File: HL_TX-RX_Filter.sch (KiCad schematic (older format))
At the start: 209 parts, among them J1 CNR1, J10 To Rx in, J11 CONN_01X03, J12 + - 12v, J2 CNR3, J3 Antenna, J4 CNR2, J5 CNR4, J6 From Tx, J7 ICSP, J8 CONN_01X05, J9 SCL SDA, Q1 2N7002, Q2 2N7002, Q3 2N7002, Q4 2N7002, Q5 2N7002, Q6 2N7002, Q7 2N7002, Q8 2N7002, U1 ATMEGA328-AU, U10 PE4259, U11 PE4259, U12 PE4259, U2 PE4259, U3 PE4259, U4 PE4259, U5 PE4259, U6 PE4259, U7 PE4259, U8 PE4259, U9 PE4259

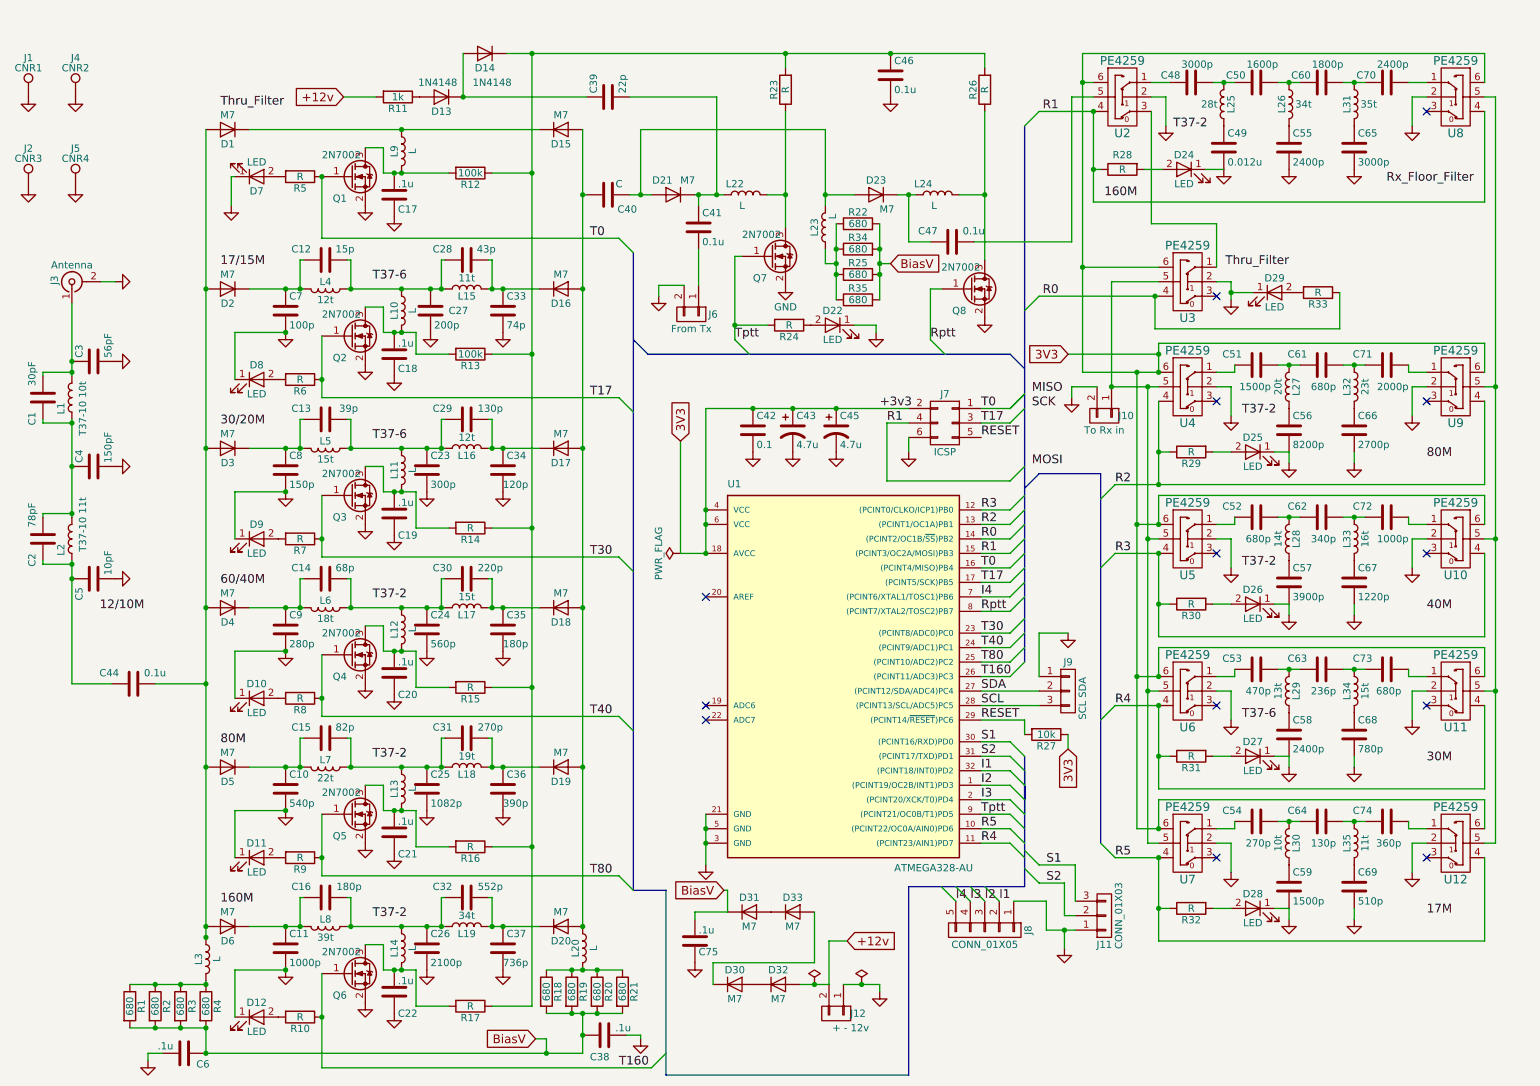
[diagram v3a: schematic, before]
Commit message: Got last of components placed on board
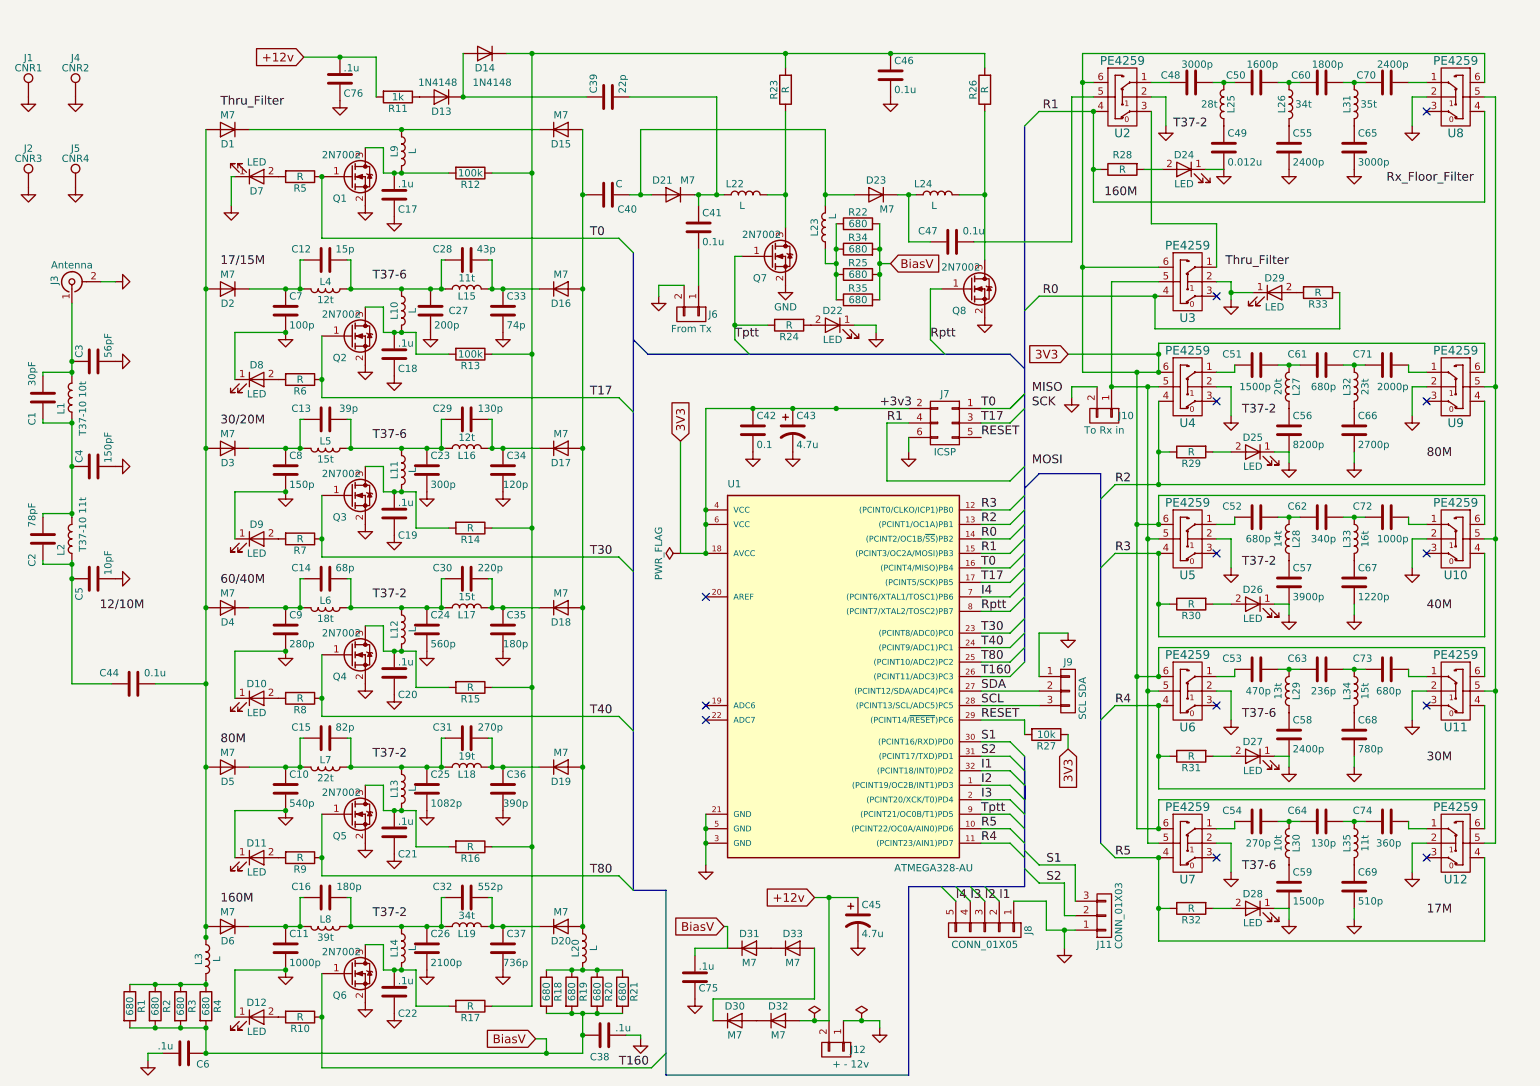
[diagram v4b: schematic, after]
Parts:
- added C76: .1u, Capacitors_SMD:C_1206_HandSoldering, symbol C
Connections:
- net +12v: now also C45.1, C76.1
- net 3V3: no longer C45.1
- net GND: now also C76.2
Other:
- moved on the sheet: C45, C75, D30, D31, D32, D33, J12
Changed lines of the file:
@@
 L PWR_FLAG #FLG050
 U 1 1 59199696
-P 6150 7025
-F 0 "#FLG050" H 6150 7100 50  0001 C CNN
-F 1 "PWR_FLAG" H 6150 7175 50  0001 C CNN
-F 2 "" H 6150 7025 50  0001 C CNN
-F 3 "" H 6150 7025 50  0001 C CNN
-	1    6150 7025
+P 6150 7275
+F 0 "#FLG050" H 6150 7350 50  0001 C CNN
+F 1 "PWR_FLAG" H 6150 7425 50  0001 C CNN
+F 2 "" H 6150 7275 50  0001 C CNN
+F 3 "" H 6150 7275 50  0001 C CNN
+	1    6150 7275
 	1    0    0    -1
 $EndComp
@@
 L CP1 C45
 U 1 1 591F53E3
-P 6300 3200
-F 0 "C45" H 6325 3300 50  0000 L CNN
-F 1 "4.7u" H 6325 3100 50  0000 L CNN
-F 2 "Capacitors_THT:CP_Radial_D5.0mm_P2.00mm" H 6300 3200 50  0001 C CNN
-F 3 "" H 6300 3200 50  0001 C CNN
-	1    6300 3200
+P 6450 6575
+F 0 "C45" H 6475 6675 50  0000 L CNN
+F 1 "4.7u" H 6475 6475 50  0000 L CNN
+F 2 "Capacitors_THT:CP_Radial_D5.0mm_P2.00mm" H 6450 6575 50  0001 C CNN
+F 3 "" H 6450 6575 50  0001 C CNN
+	1    6450 6575
 	1    0    0    -1
 $EndComp
@@
 L GND #PWR055
 U 1 1 591F5DC7
-P 6300 3350
-F 0 "#PWR055" H 6300 3100 50  0001 C CNN
-F 1 "GND" H 6300 3200 50  0001 C CNN
-F 2 "" H 6300 3350 50  0001 C CNN
-F 3 "" H 6300 3350 50  0001 C CNN
-	1    6300 3350
+P 6450 6725
+F 0 "#PWR055" H 6450 6475 50  0001 C CNN
+F 1 "GND" H 6450 6575 50  0001 C CNN
+F 2 "" H 6450 6725 50  0001 C CNN
+F 3 "" H 6450 6725 50  0001 C CNN
+	1    6450 6725
 	1    0    0    -1
 $EndComp
@@
 	5600 2000 5600 2575
 Wire Wire Line
-	2900 900  3125 900
+	3125 625  3125 900
 Wire Bus Line
 	5000 2675 7500 2675
@@
 L D D31
 U 1 1 5981B932
-P 5700 6525
-F 0 "D31" H 5700 6625 50  0000 C CNN
-F 1 "M7" H 5700 6425 50  0000 C CNN
-F 2 "Diodes_SMD:D_SMA" H 5700 6525 50  0001 C CNN
-F 3 "" H 5700 6525 50  0001 C CNN
-	1    5700 6525
+P 5700 6775
+F 0 "D31" H 5700 6875 50  0000 C CNN
+F 1 "M7" H 5700 6675 50  0000 C CNN
+F 2 "Diodes_SMD:D_SMA" H 5700 6775 50  0001 C CNN
+F 3 "" H 5700 6775 50  0001 C CNN
+	1    5700 6775
 	1    0    0    -1
 $EndComp
@@
 L D D33
 U 1 1 5981C0B2
-P 6000 6525
-F 0 "D33" H 6000 6625 50  0000 C CNN
-F 1 "M7" H 6000 6425 50  0000 C CNN
-F 2 "Diodes_SMD:D_SMA" H 6000 6525 50  0001 C CNN
-F 3 "" H 6000 6525 50  0001 C CNN
-	1    6000 6525
+P 6000 6775
+F 0 "D33" H 6000 6875 50  0000 C CNN
+F 1 "M7" H 6000 6675 50  0000 C CNN
+F 2 "Diodes_SMD:D_SMA" H 6000 6775 50  0001 C CNN
+F 3 "" H 6000 6775 50  0001 C CNN
+	1    6000 6775
 	1    0    0    -1
 $EndComp
@@
 L D D30
 U 1 1 5981C347
-P 5600 7025
-F 0 "D30" H 5600 7125 50  0000 C CNN
-F 1 "M7" H 5600 6925 50  0000 C CNN
-F 2 "Diodes_SMD:D_SMA" H 5600 7025 50  0001 C CNN
-F 3 "" H 5600 7025 50  0001 C CNN
-	1    5600 7025
+P 5600 7275
+F 0 "D30" H 5600 7375 50  0000 C CNN
+F 1 "M7" H 5600 7175 50  0000 C CNN
+F 2 "Diodes_SMD:D_SMA" H 5600 7275 50  0001 C CNN
+F 3 "" H 5600 7275 50  0001 C CNN
+	1    5600 7275
 	1    0    0    -1
 $EndComp
@@
 L D D32
 U 1 1 5981C5FF
-P 5900 7025
-F 0 "D32" H 5900 7125 50  0000 C CNN
-F 1 "M7" H 5900 6925 50  0000 C CNN
-F 2 "Diodes_SMD:D_SMA" H 5900 7025 50  0001 C CNN
-F 3 "" H 5900 7025 50  0001 C CNN
-	1    5900 7025
-	1    0    0    -1
-$EndComp
-Wire Wire Line
-	6150 6525 6150 6875
-Wire Wire Line
-	6150 6875 5450 6875
-Wire Wire Line
-	5450 6875 5450 7025
+P 5900 7275
+F 0 "D32" H 5900 7375 50  0000 C CNN
+F 1 "M7" H 5900 7175 50  0000 C CNN
+F 2 "Diodes_SMD:D_SMA" H 5900 7275 50  0001 C CNN
+F 3 "" H 5900 7275 50  0001 C CNN
+	1    5900 7275
+	1    0    0    -1
+$EndComp
+Wire Wire Line
+	6150 6775 6150 7125
+Wire Wire Line
+	6150 7125 5450 7125
+Wire Wire Line
+	5450 7125 5450 7275
 $Comp
 L CONN_01X02 J12
 U 1 1 5981CFA2
-P 6300 7225
-F 0 "J12" V 6300 7375 50  0000 C CNN
-F 1 "+ -  12v" V 6400 7325 50  0000 C CNN
-F 2 "Pin_Headers:Pin_Header_Straight_1x02_Pitch2.54mm" H 6300 7225 50  0001 C CNN
-F 3 "" H 6300 7225 50  0001 C CNN
-	1    6300 7225
+P 6300 7475
+F 0 "J12" V 6300 7625 50  0000 C CNN
+F 1 "+ -  12v" V 6400 7575 50  0000 C CNN
+F 2 "Pin_Headers:Pin_Header_Straight_1x02_Pitch2.54mm" H 6300 7475 50  0001 C CNN
+F 3 "" H 6300 7475 50  0001 C CNN
+	1    6300 7475
 	0    1    1    0
 $EndComp
 Wire Wire Line
-	6050 7025 6250 7025
+	6050 7275 6250 7275
 $Comp
 L GND #PWR076
 U 1 1 5981F912
-P 6600 7075
-F 0 "#PWR076" H 6600 6825 50  0001 C CNN
-F 1 "GND" H 6600 6925 50  0001 C CNN
-F 2 "" H 6600 7075 50  0001 C CNN
-F 3 "" H 6600 7075 50  0001 C CNN
-	1    6600 7075
+P 6600 7325
+F 0 "#PWR076" H 6600 7075 50  0001 C CNN
+F 1 "GND" H 6600 7175 50  0001 C CNN
+F 2 "" H 6600 7325 50  0001 C CNN
+F 3 "" H 6600 7325 50  0001 C CNN
+	1    6600 7325
 	-1   0    0    -1
 $EndComp
 Wire Wire Line
-	6350 7025 6600 7025
-Wire Wire Line
-	6600 7025 6600 7075
-Connection ~ 6150 7025
-Text GLabel 5525 6375 0    60   Input ~ 0
+	6350 7275 6600 7275
+Wire Wire Line
+	6600 7275 6600 7325
+Connection ~ 6150 7275
+Text GLabel 5525 6625 0    60   Input ~ 0
 BiasV
-Text GLabel 6375 6725 2    60   Input ~ 0
+Text GLabel 6150 6425 0    60   Input ~ 0
 +12v
 Wire Wire Line
-	6375 6725 6250 6725
-Wire Wire Line
-	6250 6725 6250 7025
-Text GLabel 2900 900  0    60   Input ~ 0
+	6150 6425 6450 6425
+Wire Wire Line
+	6250 7275 6250 6425
+Text GLabel 2625 625  0    60   Input ~ 0
 +12v
 $Comp
 L C C75
 U 1 1 5982474A
-P 5325 6725
-F 0 "C75" H 5350 6650 50  0000 L CNN
-F 1 ".1u" H 5350 6800 50  0000 L CNN
-F 2 "Capacitors_SMD:C_1206_HandSoldering" H 5363 6575 50  0001 C CNN
-F 3 "" H 5325 6725 50  0001 C CNN
-	1    5325 6725
+P 5325 6975
+F 0 "C75" H 5350 6900 50  0000 L CNN
+F 1 ".1u" H 5350 7050 50  0000 L CNN
+F 2 "Capacitors_SMD:C_1206_HandSoldering" H 5363 6825 50  0001 C CNN
+F 3 "" H 5325 6975 50  0001 C CNN
+	1    5325 6975
 	1    0    0    -1
 $EndComp
@@
 L GND #PWR077
 U 1 1 5982580B
-P 5325 6875
-F 0 "#PWR077" H 5325 6625 50  0001 C CNN
-F 1 "GND" H 5325 6725 50  0001 C CNN
-F 2 "" H 5325 6875 50  0001 C CNN
-F 3 "" H 5325 6875 50  0001 C CNN
-	1    5325 6875
+P 5325 7125
+F 0 "#PWR077" H 5325 6875 50  0001 C CNN
+F 1 "GND" H 5325 6975 50  0001 C CNN
+F 2 "" H 5325 7125 50  0001 C CNN
+F 3 "" H 5325 7125 50  0001 C CNN
+	1    5325 7125
 	-1   0    0    -1
 $EndComp
 Wire Wire Line
-	5550 6525 5325 6525
-Wire Wire Line
-	5325 6525 5325 6575
-Wire Wire Line
-	5550 6525 5550 6375
-Wire Wire Line
-	5550 6375 5525 6375
+	5550 6775 5325 6775
+Wire Wire Line
+	5325 6775 5325 6825
+Wire Wire Line
+	5550 6775 5550 6625
+Wire Wire Line
+	5550 6625 5525 6625
 $Comp
 L PWR_FLAG #FLG078
 U 1 1 598278BA
-P 6475 7025
-F 0 "#FLG078" H 6475 7100 50  0001 C CNN
-F 1 "PWR_FLAG" H 6475 7175 50  0001 C CNN
-F 2 "" H 6475 7025 50  0001 C CNN
-F 3 "" H 6475 7025 50  0001 C CNN
-	1    6475 7025
-	1    0    0    -1
-$EndComp
-Connection ~ 6475 7025
+P 6475 7275
+F 0 "#FLG078" H 6475 7350 50  0001 C CNN
+F 1 "PWR_FLAG" H 6475 7425 50  0001 C CNN
+F 2 "" H 6475 7275 50  0001 C CNN
+F 3 "" H 6475 7275 50  0001 C CNN
+	1    6475 7275
+	1    0    0    -1
+$EndComp
+Connection ~ 6475 7275
+Connection ~ 6250 6425
+$Comp
+L C C76
+U 1 1 59810339
+P 2875 775
+F 0 "C76" H 2900 675 50  0000 L CNN
+F 1 ".1u" H 2900 850 50  0000 L CNN
+F 2 "Capacitors_SMD:C_1206_HandSoldering" H 2913 625 50  0001 C CNN
+F 3 "" H 2875 775 50  0001 C CNN
+	1    2875 775
+	1    0    0    -1
+$EndComp
+$Comp
+L GND #PWR079
+U 1 1 5981033F
+P 2875 925
+F 0 "#PWR079" H 2875 675 50  0001 C CNN
+F 1 "GND" H 2875 775 50  0001 C CNN
+F 2 "" H 2875 925 50  0001 C CNN
+F 3 "" H 2875 925 50  0001 C CNN
+	1    2875 925
+	1    0    0    -1
+$EndComp
+Wire Wire Line
+	2625 625  3125 625
+Connection ~ 2875 625
+Text Label 9100 6250 0    60   ~ 0
+T37-6
 $EndSCHEMATC

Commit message: Reorganizing the components after annotate done
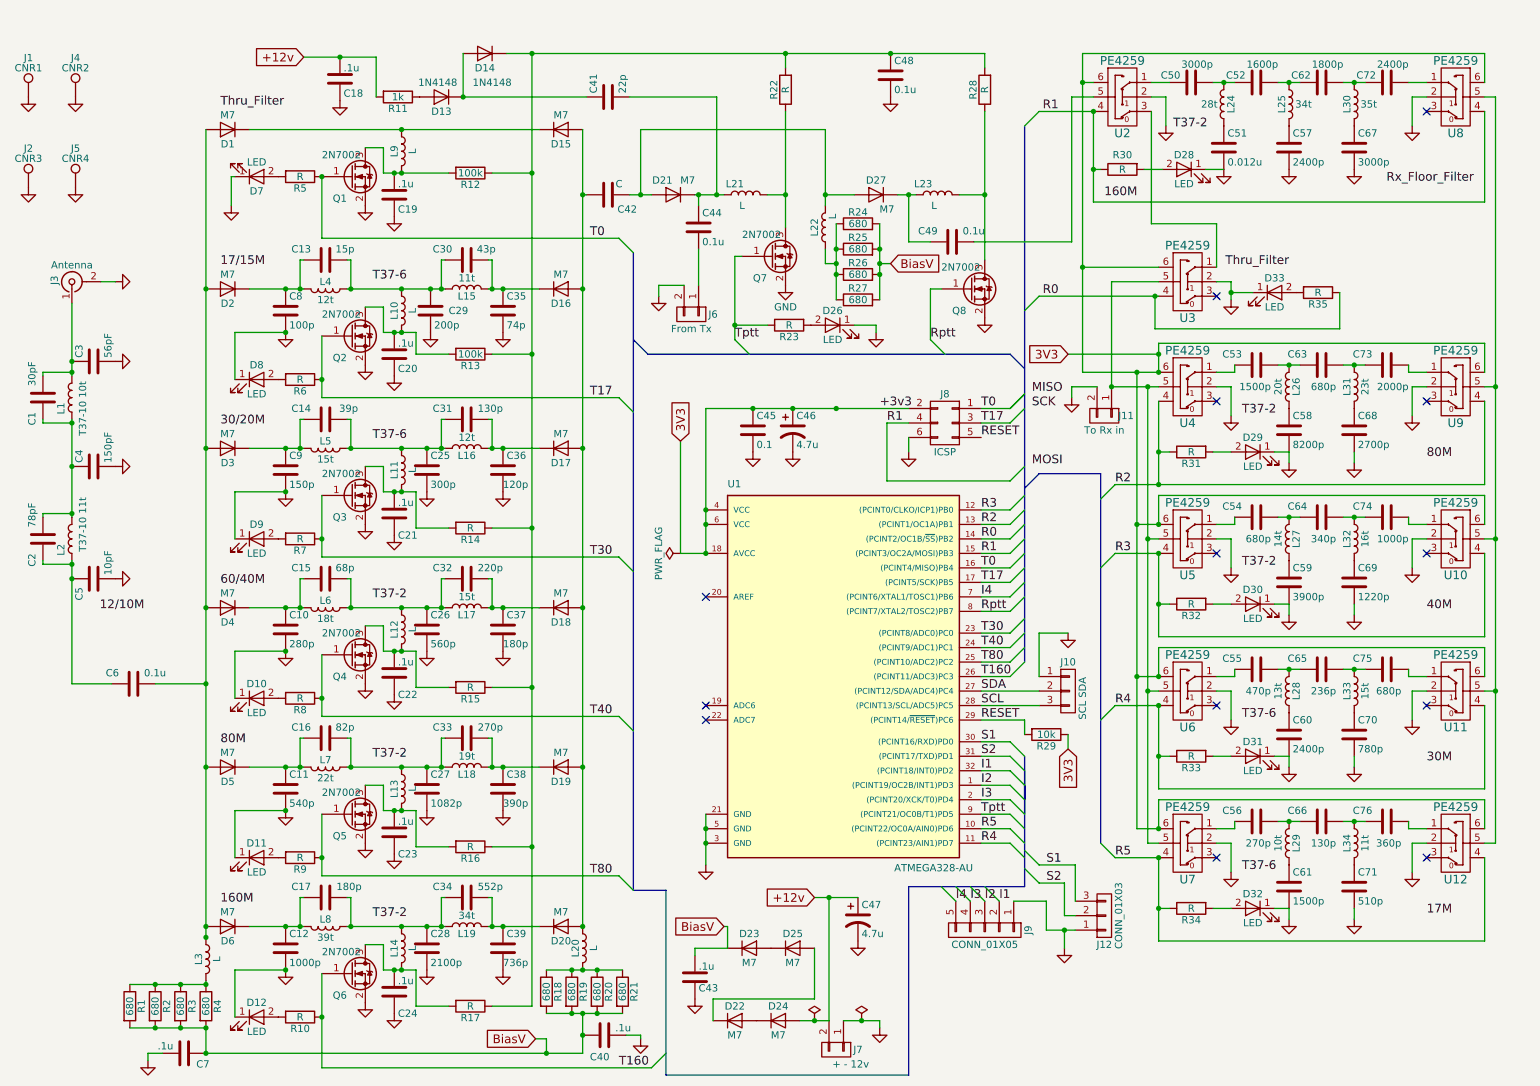
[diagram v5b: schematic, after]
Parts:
- renumbered C9 to C10, C10 to C11, C11 to C12, C12 to C13, C13 to C14, C14 to C15, C15 to C16, C16 to C17, C76 to C18, C17 to C19, C18 to C20, C19 to C21, C20 to C22, C21 to C23, C22 to C24, C23 to C25, C24 to C26, C25 to C27, C26 to C28, C27 to C29, C28 to C30, C29 to C31, C30 to C32, C31 to C33, C32 to C34, C33 to C35, C34 to C36, C35 to C37, C36 to C38, C37 to C39, C38 to C40, C39 to C41, C40 to C42, C75 to C43, C41 to C44, C42 to C45, C43 to C46, C45 to C47, C46 to C48, C47 to C49, C48 to C50, C49 to C51, C50 to C52, C51 to C53, C52 to C54, C53 to C55, C54 to C56, C55 to C57, C56 to C58, C57 to C59, C44 to C6, C58 to C60, C59 to C61, C60 to C62, C61 to C63, C62 to C64, C63 to C65, C64 to C66, C65 to C67, C66 to C68, C67 to C69, C6 to C7, C68 to C70, C69 to C71, C70 to C72, C71 to C73, C72 to C74, C73 to C75, C74 to C76, C7 to C8, C8 to C9, D30 to D22, D31 to D23, D32 to D24, D33 to D25, D22 to D26, D23 to D27, D24 to D28, D25 to D29, D26 to D30, D27 to D31, D28 to D32, D29 to D33, J9 to J10, J10 to J11, J11 to J12, J12 to J7, J7 to J8, J8 to J9, L22 to L21, L23 to L22, L24 to L23, L25 to L24, L26 to L25, L27 to L26, L28 to L27, L29 to L28, L30 to L29, L31 to L30, L32 to L31, L33 to L32, L34 to L33, L35 to L34, R23 to R22, R24 to R23, R22 to R24, R34 to R25, R25 to R26, R35 to R27, R26 to R28, R27 to R29, R28 to R30, R29 to R31, R30 to R32, R31 to R33, R32 to R34, R33 to R35
